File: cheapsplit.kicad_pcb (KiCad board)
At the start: 2 copper layers, 94 x 91 mm, 51 parts, among them J1 AudioJack4, SW1 SW_Push, SW10 SW_Push, SW11 SW_Push, SW12 SW_Push, SW13 SW_Push, SW14 SW_Push, SW15 SW_Push, SW16 SW_Push, SW17 SW_Push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

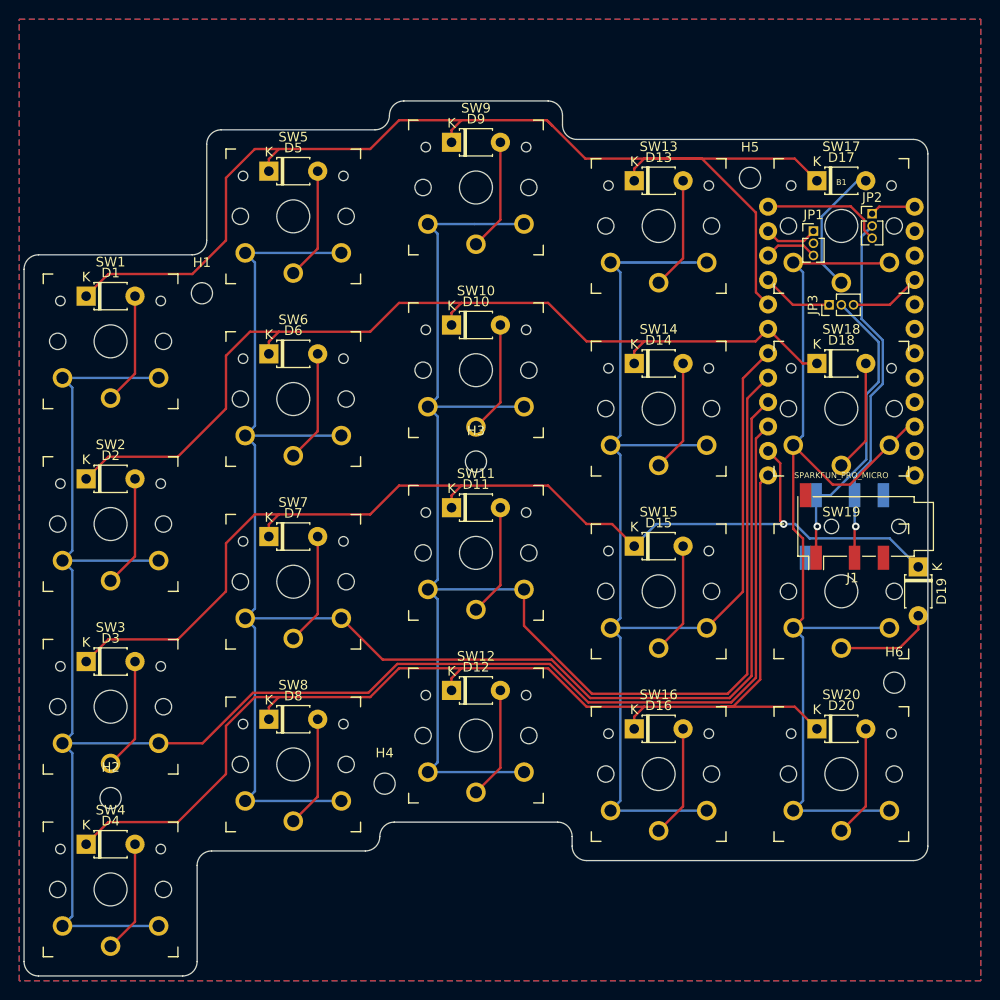
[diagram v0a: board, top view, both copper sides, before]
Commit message: Removed silkscreen
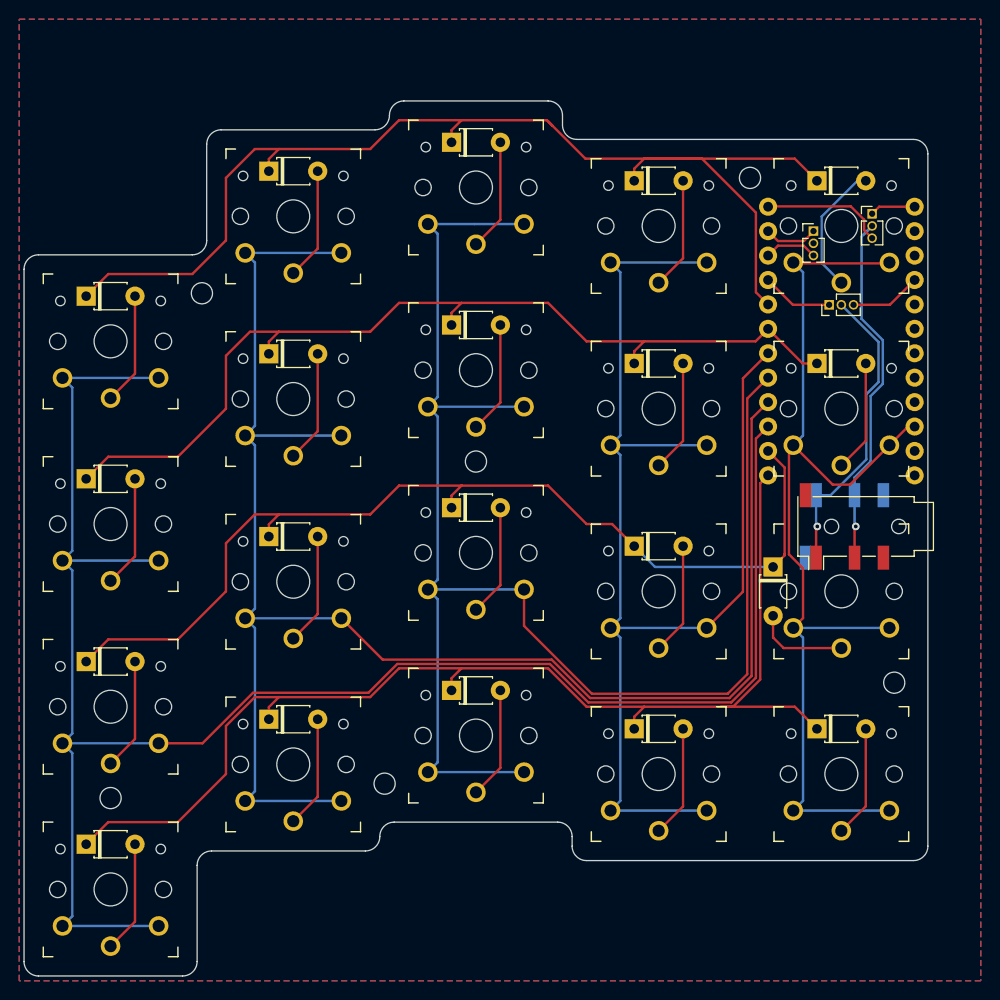
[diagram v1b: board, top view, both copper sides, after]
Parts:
- moved D19 15.1 mm to (178.4, 107.0)
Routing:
- net row2: track 116.2 -> 104.2 mm, vias 1 -> 0
